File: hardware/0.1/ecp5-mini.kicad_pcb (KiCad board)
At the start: 4 copper layers, 52 x 27 mm, 102 parts, among them J1 Micro_SD_Card, J2 JTAG, J3 S7 Mini, J4 S7 Mini, J5 USB_C_Receptacle_USB2.0, Q1 BSS138, Q2 BSS138, Q3 BSS138, Q4 BSS138, SW1 SW_Push, U1 ECP5U_12_CABGA256, U2 TLV73325PDBV, U3 TLV62568DBV, U4 USBLC6-2SC6, U5 TLV62568DBV, U6 W25Q128JVSIQ, U7 S27KL0641, X1 DSC6101CI2A-016

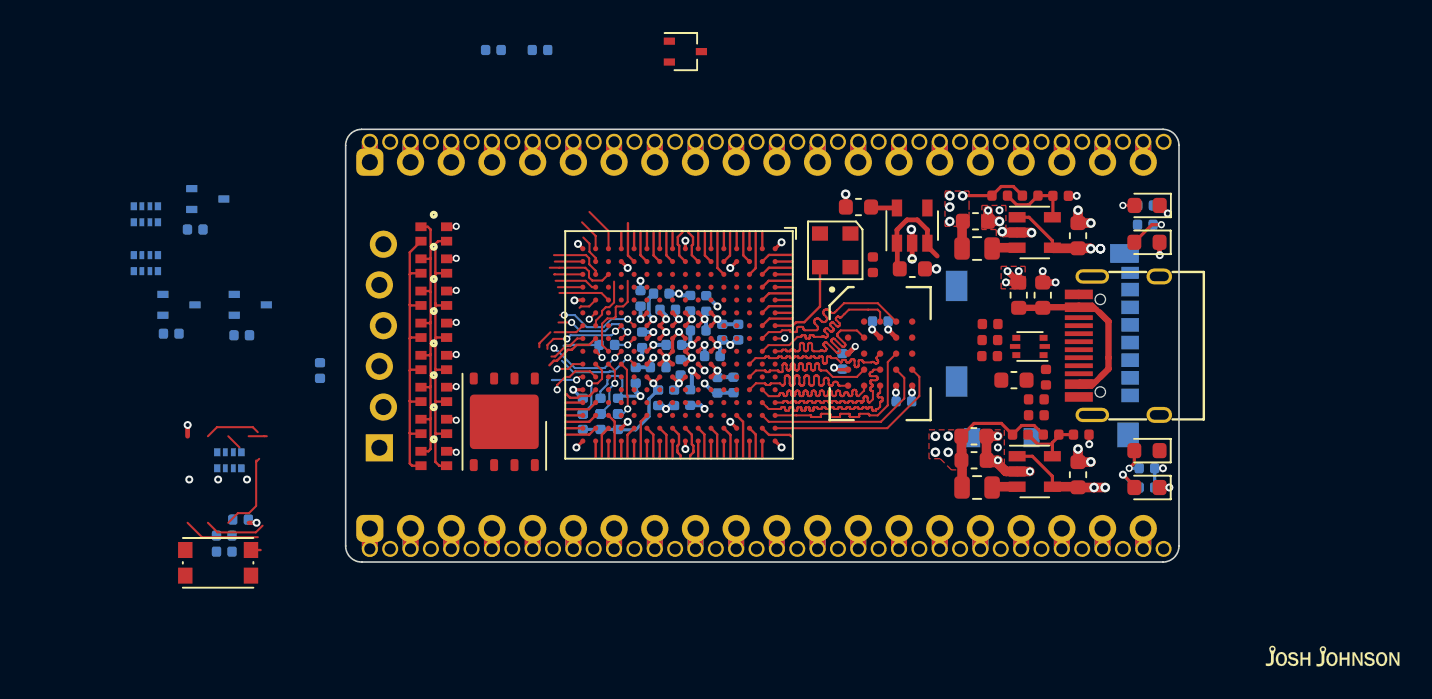
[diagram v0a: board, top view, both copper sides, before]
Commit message: half IO laid out
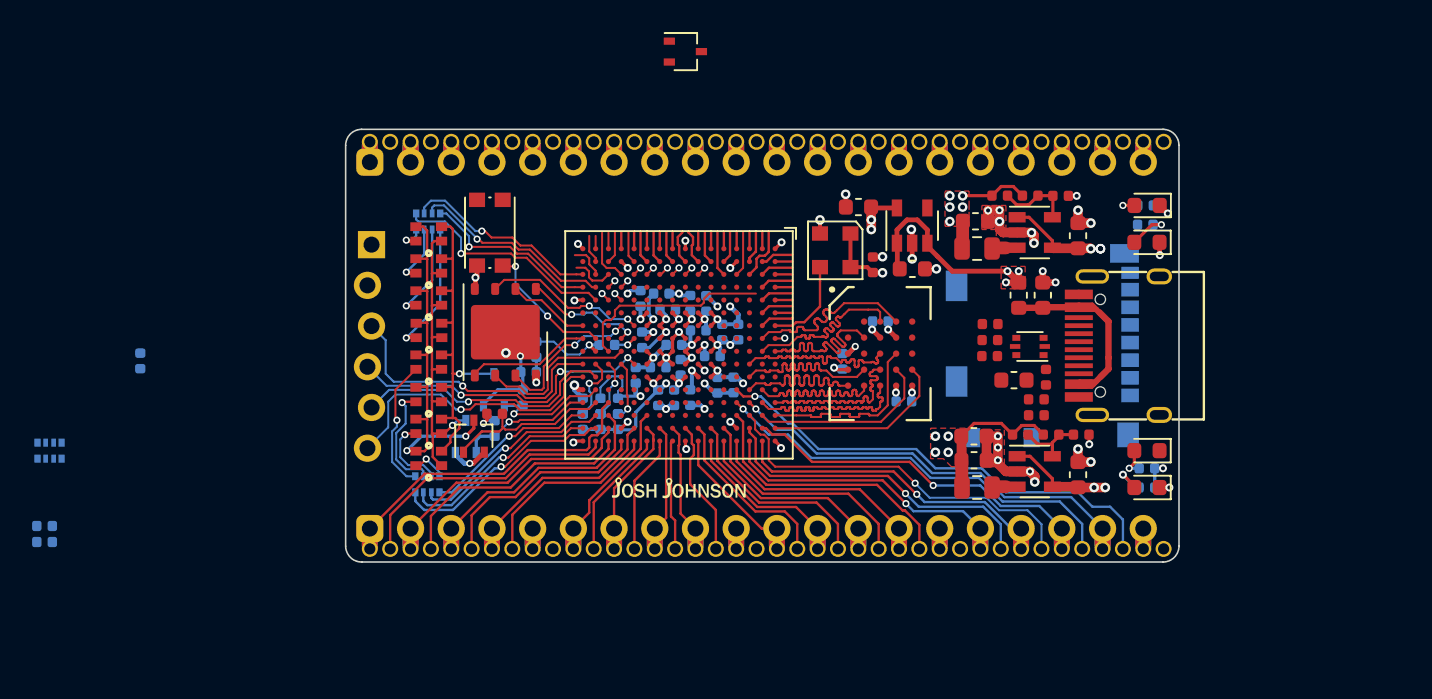
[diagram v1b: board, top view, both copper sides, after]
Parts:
- removed R34: 1K5, Resistor_SMD:R_0402_1005Metric
- added R23: 1K5, Resistor_SMD:R_0402_1005Metric, B.Cu at (146.1, 87.4)
- Q4, R30: moved to F.Cu
- moved LOGO1 42.1 mm to (117.0, 103.8)
- moved SW1 26.7 mm to (105.2, 87.9), turned to 90 degrees
- moved RN2 24.3 mm to (101.3, 103.6)
- moved R28 22.4 mm to (105.5, 100.1), turned to 90 degrees
- moved R25 22.3 mm to (107.2, 98.2), turned to 90 degrees
- moved Q3 21.9 mm to (103.7, 100.6), turned to 90 degrees
- moved Q2 20.4 mm to (105.5, 97.7), turned to 90 degrees
- moved C18 20.2 mm to (107.6, 96.6)
- moved R19 18.7 mm to (108.1, 95.2), turned to 90 degrees
- moved C15 18.2 mm to (106.7, 94.7), turned to 180 degrees
- moved RN3 17.8 mm to (101.3, 87.2), turned to 90 degrees
- moved R30 16.5 mm to (105.5, 99.2), turned to 180 degrees
- moved Q4 16.2 mm to (104.2, 100.6), turned to 90 degrees
- moved J2 12.7 mm to (97.7, 88.6), turned to 0 degrees
- moved D10 12.0 mm to (101.4, 90.0), turned to -90 degrees
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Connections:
- net /FPGA Config/CFG.CLK renamed /FPGA Config/CFG_CLK
- net /FPGA Config/CFG.CS renamed /FPGA Config/CFG_CS
- net /FPGA Config/CFG.IO0 renamed /FPGA Config/CFG_IO0
- net /FPGA Config/CFG.IO1 renamed /FPGA Config/CFG_IO1
- net /FPGA Config/CFG.IO2 renamed /FPGA Config/CFG_IO2
- net /FPGA Config/CFG.IO3 renamed /FPGA Config/CFG_IO3
- J4 pad 1: /PORT_G0 -> /PORT_H0
- J4 pad 2: /PORT_G4 -> /PORT_H4
- J4 pad 3: /PORT_G1 -> /PORT_H1
- J4 pad 4: /PORT_G5 -> /PORT_H5
- J4 pad 5: /PORT_G2 -> /PORT_H2
- J4 pad 6: /PORT_G6 -> /PORT_H6
- J4 pad 7: /PORT_G3 -> /PORT_H3
- J4 pad 8: /PORT_G7 -> /PORT_H7
- Q4 pad 3: /LEDs/CAT_G -> /LEDs/CAT_B
- R22 pad 1: /FPGA Config/LED_USR -> /LED_USR
- RN2 pad 5: /LEDs/LED_0 -> /LED_0
- RN2 pad 6: /LEDs/LED_1 -> /LED_1
- RN2 pad 7: /LEDs/LED_2 -> /LED_2
- RN2 pad 8: /LEDs/LED_3 -> /LED_3
- RN3 pad 1: Net-(D11-Pad4) -> Net-(D8-Pad4)
- RN3 pad 2: Net-(D10-Pad4) -> Net-(D9-Pad4)
- RN3 pad 3: Net-(D9-Pad4) -> Net-(D10-Pad4)
- RN3 pad 4: Net-(D8-Pad4) -> Net-(D11-Pad4)
- RN3 pad 5: /LEDs/LED_4 -> /LED_7
- RN3 pad 6: /LEDs/LED_5 -> /LED_6
- RN3 pad 7: /LEDs/LED_6 -> /LED_5
- RN3 pad 8: /LEDs/LED_7 -> /LED_4
- U1 pad B15: Net-(U1-PadB15) -> /PORT_D2
- U1 pad B16: Net-(U1-PadB16) -> /PORT_D1
- U1 pad C13: Net-(U1-PadC13) -> /PORT_D3
- U1 pad C14: Net-(U1-PadC14) -> /PORT_D5
- U1 pad C15: Net-(U1-PadC15) -> /PORT_D4
- U1 pad C16: Net-(U1-PadC16) -> /PORT_D0
- U1 pad D12: Net-(U1-PadD12) -> /PORT_D7
- U1 pad D13: Net-(U1-PadD13) -> /PORT_D6
- U1 pad D14: Net-(U1-PadD14) -> /PORT_C7
- U1 pad D16: Net-(U1-PadD16) -> /PORT_C3
- U1 pad E15: Net-(U1-PadE15) -> /PORT_C6
- U1 pad E16: Net-(U1-PadE16) -> /PORT_C2
- U1 pad F15: Net-(U1-PadF15) -> /PORT_C5
- U1 pad F16: Net-(U1-PadF16) -> /PORT_C1
- U1 pad G15: Net-(U1-PadG15) -> /PORT_C4
- U1 pad G16: Net-(U1-PadG16) -> /PORT_C0
- U1 pad H15: Net-(U1-PadH15) -> /PORT_B7
- U1 pad J15: Net-(U1-PadJ15) -> /PORT_B3
- U1 pad J16: Net-(U1-PadJ16) -> /PORT_B6
- U1 pad K15: Net-(U1-PadK15) -> /PORT_B2
- U1 pad K16: Net-(U1-PadK16) -> /PORT_B5
- U1 pad L14: Net-(U1-PadL14) -> /PORT_B0
- U1 pad L15: Net-(U1-PadL15) -> /PORT_B1
- U1 pad L16: Net-(U1-PadL16) -> /PORT_B4
- U1 pad M15: Net-(U1-PadM15) -> /PORT_A3
- U1 pad M16: Net-(U1-PadM16) -> /PORT_A7
- U1 pad N16: Net-(U1-PadN16) -> /PORT_A6
- U1 pad P13: Net-(U1-PadP13) -> /PORT_A0
- U1 pad P14: Net-(U1-PadP14) -> /PORT_A2
- U1 pad P15: Net-(U1-PadP15) -> /PORT_A1
- U1 pad P16: Net-(U1-PadP16) -> /PORT_A5
- U1 pad P9: /FPGA Config/CFG.CDONE -> /FPGA Config/CFG_CDONE
- U1 pad R12: Net-(U1-PadR12) -> /LED_R
- U1 pad R13: Net-(U1-PadR13) -> /LED_B
- U1 pad R14: Net-(U1-PadR14) -> /LED_1
- U1 pad R15: Net-(U1-PadR15) -> /LED_3
- U1 pad R16: Net-(U1-PadR16) -> /PORT_A4
- U1 pad R4: Net-(U1-PadR4) -> /LED_5
- U1 pad R5: Net-(U1-PadR5) -> /LED_7
- U1 pad R6: /FPGA Config/FPGA_OK -> Net-(U1-PadR6)
- U1 pad R7: /FPGA Config/LED_USR -> Net-(U1-PadR7)
- U1 pad T13: Net-(U1-PadT13) -> /LED_G
- U1 pad T14: Net-(U1-PadT14) -> /LED_0
- U1 pad T15: Net-(U1-PadT15) -> /LED_2
- U1 pad T3: Net-(U1-PadT3) -> /LED_6
- U1 pad T4: Net-(U1-PadT4) -> /LED_4
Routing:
- net /PORT_D7: track 0.00 -> 29.3 mm, vias 0 -> 1
- net /PORT_D6: track 0.00 -> 26.3 mm, vias 0 -> 1
- net +1V1: track 21.1 -> 47.3 mm, vias 9 -> 8
- net /PORT_D3: track 0.00 -> 25.3 mm, vias 0 -> 1
- net +2V5: track 5.85 -> 30.8 mm, vias 2 -> 4
- net /PORT_D5: track 0.00 -> 23.7 mm, vias 0 -> 1
- net /PORT_D2: track 0.00 -> 21.3 mm, vias 0 -> 1
- net /PORT_D4: track 0.00 -> 20.7 mm, vias 0 -> 1
- net GND: track 62.7 -> 82.7 mm, vias 60 -> 63
- net /PORT_A0: track 0.00 -> 19.3 mm
- net /PORT_D1: track 0.00 -> 19.2 mm, vias 0 -> 1
- net /PORT_D0: track 0.00 -> 17.4 mm, vias 0 -> 1
- net /PORT_C7: track 0.00 -> 17.2 mm
- net /PORT_A4: track 0.00 -> 17.1 mm
- net /FPGA Config/TCK: track 1.88 -> 17.9 mm
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- added copper zone on In2.Cu, net +1V1

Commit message: half IO routed
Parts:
- Q1, R11: moved to B.Cu
- moved Q1 35.6 mm to (142.8, 101.5)
- moved R12 33.7 mm to (108.1, 93.2), turned to 90 degrees
- moved C13 32.4 mm to (107.1, 93.2), turned to -90 degrees
- moved RN1 28.8 mm to (105.3, 93.2)
- moved R8 21.5 mm to (104.8, 94.8), turned to 0 degrees
- moved LOGO2 20.0 mm to (154.3, 91.8)
- moved R11 3.54 mm to (132.9, 93.8)
- moved R7 1.00 mm to (139.3, 99.3)
- moved R6 0.99 mm to (139.3, 98.3)
- moved C11 0.67 mm to (137.6, 97.7), turned to -90 degrees
- moved C12 0.65 mm to (139.3, 96.7), turned to 0 degrees
- moved C25 0.35 mm to (119.2, 97.7)
- moved C29 0.35 mm to (120.2, 97.7)
- moved R19 0.10 mm to (108.2, 95.2)
- moved C15 0.10 mm to (106.7, 94.8)
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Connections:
- J1 pad 10: /SD_DETA -> /SD_DET
- J1 pad 9: /SD_DETB -> GND
- Q1 pad 1: /FPGA Config/CFG.CDONE -> /FPGA Config/CFG_CDONE
- RN1 pad 1: /FPGA Config/CFG_CS -> /FPGA Config/CFG_IO3
- RN1 pad 2: /FPGA Config/CFG_IO1 -> /FPGA Config/CFG_CLK
- RN1 pad 4: /FPGA Config/CFG_IO3 -> /FPGA Config/CFG_CS
- U1 pad A8: Net-(U1-PadA8) -> /USB_PU
- U1 pad B15: /PORT_D2 -> /PORT_D3
- U1 pad B16: /PORT_D1 -> /PORT_D7
- U1 pad C13: /PORT_D3 -> /SD_DAT3
- U1 pad C14: /PORT_D5 -> /PORT_D6
- U1 pad C15: /PORT_D4 -> /PORT_D1
- U1 pad C16: /PORT_D0 -> /PORT_D5
- U1 pad D10: Net-(U1-PadD10) -> /SD_DAT0
- U1 pad D12: /PORT_D7 -> /SD_CLK
- U1 pad D13: /PORT_D6 -> /SD_CMD
- U1 pad D14: /PORT_C7 -> /PORT_D2
- U1 pad D16: /PORT_C3 -> /PORT_D4
- U1 pad D9: Net-(U1-PadD9) -> /USB_D-
- U1 pad E10: Net-(U1-PadE10) -> /SD_DAT1
- U1 pad E12: Net-(U1-PadE12) -> /SD_DET
- U1 pad E13: Net-(U1-PadE13) -> /SD_DAT2
- U1 pad E15: /PORT_C6 -> /PORT_D0
- U1 pad E16: /PORT_C2 -> /PORT_C3
- U1 pad E9: Net-(U1-PadE9) -> /USB_D+
- U1 pad F15: /PORT_C5 -> /PORT_C7
- U1 pad F16: /PORT_C1 -> /PORT_C5
- U1 pad G14: Net-(U1-PadG14) -> /PORT_C6
- U1 pad G15: /PORT_C4 -> /PORT_C1
- U1 pad G16: /PORT_C0 -> /PORT_C4
- U1 pad H14: Net-(U1-PadH14) -> /PORT_C2
- U1 pad H15: /PORT_B7 -> /PORT_C0
- U1 pad J14: Net-(U1-PadJ14) -> /PORT_B7
- U1 pad J15: /PORT_B3 -> /PORT_B2
- U1 pad K14: Net-(U1-PadK14) -> /PORT_B3
- U1 pad K15: /PORT_B2 -> /PORT_B1
- U1 pad L14: /PORT_B0 -> Net-(U1-PadL14)
- U1 pad L15: /PORT_B1 -> /PORT_B0
- U1 pad P13: /PORT_A0 -> /LED_G
- U1 pad P14: /PORT_A2 -> /LED_3
- U1 pad P15: /PORT_A1 -> /PORT_A2
- U1 pad R13: /LED_B -> /LED_0
- U1 pad R14: /LED_1 -> /LED_2
- U1 pad R15: /LED_3 -> /PORT_A4
- U1 pad R16: /PORT_A4 -> /PORT_A1
- U1 pad T13: /LED_G -> /LED_B
- U1 pad T14: /LED_0 -> /LED_1
- U1 pad T15: /LED_2 -> /PORT_A0
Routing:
- net /FPGA Config/CFG_CDONE: track 12.6 -> 50.2 mm, vias 0 -> 5
- net /SD_DAT1: track 0.00 -> 30.7 mm, vias 0 -> 1
- net /SD_DAT0: track 0.00 -> 28.9 mm, vias 0 -> 1
- net GND: track 82.7 -> 111.4 mm, vias 63 -> 67
- net /SD_CLK: track 0.00 -> 27.6 mm, vias 0 -> 1
- net /SD_DAT2: track 0.00 -> 27.3 mm, vias 0 -> 1
- net /SD_CMD: track 0.00 -> 26.9 mm, vias 0 -> 1
- net /SD_DAT3: track 0.00 -> 25.5 mm, vias 0 -> 1
- net /USB_D+: track 0.00 -> 20.2 mm, vias 0 -> 2
- net +3V3: track 39.5 -> 58.6 mm, vias 21 -> 24
- net /USB_D-: track 0.00 -> 18.8 mm, vias 0 -> 2
- net /SD_DET: track 0.00 -> 18.1 mm, vias 0 -> 1
- net Net-(J5-PadB5): track 0.00 -> 17.0 mm, vias 0 -> 4
- net /USB_PU: track 0.00 -> 12.3 mm, vias 0 -> 1
- net /FPGA Config/CFG_CLK: track 10.2 -> 21.3 mm, vias 0 -> 1
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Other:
- board text added: "3V3"
- board text added: "5V0"
- board text added: "GND"
- board text added: "PR11C+"
- board text added: "PR11D-"
- board text added: "PR14A+"
- board text added: "PR14B-"
- board text added: "PR14C+"
- board text added: "PR14D-"
- board text added: "PR20A+"
- board text added: "PR20B-"
- board text added: "PR20C+"
- board text added: "PR20D-"
- board text added: "PR23A+"
- board text added: "PR23B-"
- board text added: "PR23C+"
- board text added: "PR23D-"
- board text added: "PR26A+"
- board text added: "PR26B-"
- board text added: "PR26C+"
- board text added: "PR26D-"
- board text added: "PR2A+"
- board text added: "PR2B-"
- board text added: "PR2C+"
- board text added: "PR2D-"
- board text added: "PR32A+"
- board text added: "PR32B-"
- board text added: "PR35A+"
- board text added: "PR35B-"
- board text added: "PR38C+"
- board text added: "PR38D-"
- board text added: "PR5A+"
- board text added: "PR5B-"
- board text added: "PR8A+"
- board text added: "PR8B-"
- board text added: "TCK"
- board text added: "TDI"
- board text added: "TDO"
- board text added: "TMS"

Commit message: unrouted = 0
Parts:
- moved LOGO2 19.0 mm to (135.4, 92.5)
- moved Q1 1.75 mm to (142.8, 103.2)
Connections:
- U1 pad A2: Net-(U1-PadA2) -> /PORT_E2
- U1 pad A3: Net-(U1-PadA3) -> /PORT_E3
- U1 pad A4: Net-(U1-PadA4) -> /PORT_E7
- U1 pad A5: Net-(U1-PadA5) -> /LED_USR
- U1 pad A6: Net-(U1-PadA6) -> /FPGA_OK
- U1 pad B1: Net-(U1-PadB1) -> /PORT_E1
- U1 pad B2: Net-(U1-PadB2) -> /PORT_E5
- U1 pad B3: Net-(U1-PadB3) -> /PORT_E6
- U1 pad C1: Net-(U1-PadC1) -> /PORT_E0
- U1 pad C2: Net-(U1-PadC2) -> /PORT_E4
- U1 pad F1: Net-(U1-PadF1) -> /PORT_F3
- U1 pad G1: Net-(U1-PadG1) -> /PORT_F2
- U1 pad G2: Net-(U1-PadG2) -> /PORT_F7
- U1 pad H2: Net-(U1-PadH2) -> /PORT_F6
- U1 pad J1: Net-(U1-PadJ1) -> /PORT_F1
- U1 pad J2: Net-(U1-PadJ2) -> /PORT_F5
- U1 pad K1: Net-(U1-PadK1) -> /PORT_F0
- U1 pad K2: Net-(U1-PadK2) -> /PORT_F4
- U1 pad L1: Net-(U1-PadL1) -> /PORT_G2
- U1 pad L2: Net-(U1-PadL2) -> /PORT_G6
- U1 pad L3: Net-(U1-PadL3) -> /PORT_G3
- U1 pad M1: Net-(U1-PadM1) -> /PORT_G1
- U1 pad M2: Net-(U1-PadM2) -> /PORT_G5
- U1 pad M3: Net-(U1-PadM3) -> /PORT_G7
- U1 pad N1: Net-(U1-PadN1) -> /PORT_G0
- U1 pad N4: Net-(U1-PadN4) -> /PORT_H2
- U1 pad P1: Net-(U1-PadP1) -> /PORT_H3
- U1 pad P2: Net-(U1-PadP2) -> /PORT_G4
- U1 pad P3: Net-(U1-PadP3) -> /PORT_H6
- U1 pad P4: Net-(U1-PadP4) -> /PORT_H1
- U1 pad R1: Net-(U1-PadR1) -> /PORT_H7
- U1 pad R2: Net-(U1-PadR2) -> /PORT_H0
- U1 pad R3: Net-(U1-PadR3) -> /PORT_H5
- U1 pad T2: Net-(U1-PadT2) -> /PORT_H4
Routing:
- net /LED_USR: track 0.00 -> 27.8 mm, vias 0 -> 1
- net /PORT_E7: track 0.00 -> 27.2 mm, vias 0 -> 1
- net /FPGA_OK: track 0.00 -> 26.2 mm, vias 0 -> 1
- net /PORT_E6: track 0.00 -> 24.6 mm, vias 0 -> 1
- net /PORT_E3: track 0.00 -> 24.2 mm, vias 0 -> 1
- net /PORT_E5: track 0.00 -> 22.7 mm, vias 0 -> 1
- net /PORT_E2: track 0.00 -> 21.4 mm, vias 0 -> 1
- net /PORT_E4: track 0.00 -> 20.8 mm, vias 0 -> 1
- net /PORT_E1: track 0.00 -> 20.6 mm, vias 0 -> 1
- net /PORT_F7: track 0.00 -> 18.0 mm
- net /PORT_E0: track 0.00 -> 17.5 mm, vias 0 -> 1
- net /PORT_H0: track 0.00 -> 17.0 mm, vias 0 -> 1
- net /PORT_F6: track 0.00 -> 16.8 mm
- net /PORT_H1: track 0.00 -> 16.4 mm, vias 0 -> 1
- net /PORT_H4: track 0.00 -> 16.3 mm, vias 0 -> 1
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- added copper zone on B.Cu, net GND
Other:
- board text added: "ACT"
- board text added: "ECP5"
- board text added: "ECP5 Mini"
- board text added: "PL14A+"
- board text added: "PL14B-"
- board text added: "PL20A+"
- board text added: "PL20B-"
- board text added: "PL23A+"
- board text added: "PL23B-"
- board text added: "PL23C+"
- board text added: "PL23D-"
- board text added: "PL26A+"
- board text added: "PL26B-"
- board text added: "PL26C+"
- board text added: "PL26D-"
- board text added: "PL2A+"
- board text added: "PL2B-"
- board text added: "PL32A+"
- board text added: "PL32B-"
- board text added: "PL32C+"
- board text added: "PL32D-"
- board text added: "PL35A+"
- board text added: "PL35B-"
- board text added: "PL38A+"
- board text added: "PL38B-"
- board text added: "PL38C+"
- board text added: "PL38D-"
- board text added: "PL41A+"
- board text added: "PL41B-"
- board text added: "PL4A+"
- board text added: "PL4B-"
- board text added: "PL5A+"
- board text added: "PL5B-"
- board text added: "PL6A+"
- board text added: "PL6B-"
- board text added: "PWR"
- board text added: "USR"

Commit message: clean up routing
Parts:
- moved R10 2.60 mm to (133.8, 94.5)
- moved R9 2.58 mm to (133.8, 95.5)
- moved R11 1.15 mm to (133.8, 94.5)
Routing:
- net /USB_D-: track 18.8 -> 14.4 mm
- net Net-(R10-Pad2): track 1.18 -> 3.78 mm
- net Net-(R9-Pad1): track 1.20 -> 3.78 mm
- net GND: track 112.3 -> 110.0 mm
- net /USB_D+: track 20.2 -> 17.9 mm
- net +5V: track 70.7 -> 72.2 mm
- net Net-(C6-Pad1): track 17.3 -> 18.8 mm
- net +3V3: track 58.6 -> 59.8 mm
- net /PORT_H2: track 15.0 -> 13.9 mm
- net /FPGA Config/nBTN_USR: track 14.4 -> 15.5 mm
- net Net-(D1-Pad2): track 2.77 -> 2.02 mm
- net /LED_5: track 12.7 -> 13.3 mm
- removed copper zone on B.Cu, net GND

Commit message: all DRC / ERC errors signed off
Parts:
- moved R11 1.98 mm to (131.9, 94.0), turned to 180 degrees
- moved R10 0.35 mm to (134.2, 94.5)
- moved R9 0.35 mm to (134.2, 95.5)
- moved Q1 0.15 mm to (142.8, 103.1)
- moved C17 0.15 mm to (114.5, 92.0)
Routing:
- net /USB_PU: track 12.4 -> 14.4 mm
